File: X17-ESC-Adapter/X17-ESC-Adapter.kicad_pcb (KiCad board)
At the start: 2 copper layers, 9 parts, among them J2 Power In/Out

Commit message: 10/12/24
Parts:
- added J2: Power In/Out, IPS1-105-01-L-D:SAMTEC_IPS1-105-01-L-D, F.Cu at (185.5, 80.0)
- moved ESC3 9.98 mm to (197.0, 87.5), turned to -90 degrees
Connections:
- ESC5 pad 5: ESC2C -> ESC2B
- ESC5 pad 6: ESC2B -> ESC2C
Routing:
- net ESC3C: track 24.3 -> 0.00 mm
- net ESC3B: track 20.4 -> 0.00 mm
- net ESC3A: track 13.5 -> 1.71 mm
- net ESC2C: track 3.77 -> 0.00 mm
- net ESC2B: track 0.00 -> 3.77 mm
- added copper zone on F.Cu, net ESC2A
- added copper zone on F.Cu, net ESC2B
- added copper zone on F.Cu, net ESC2C

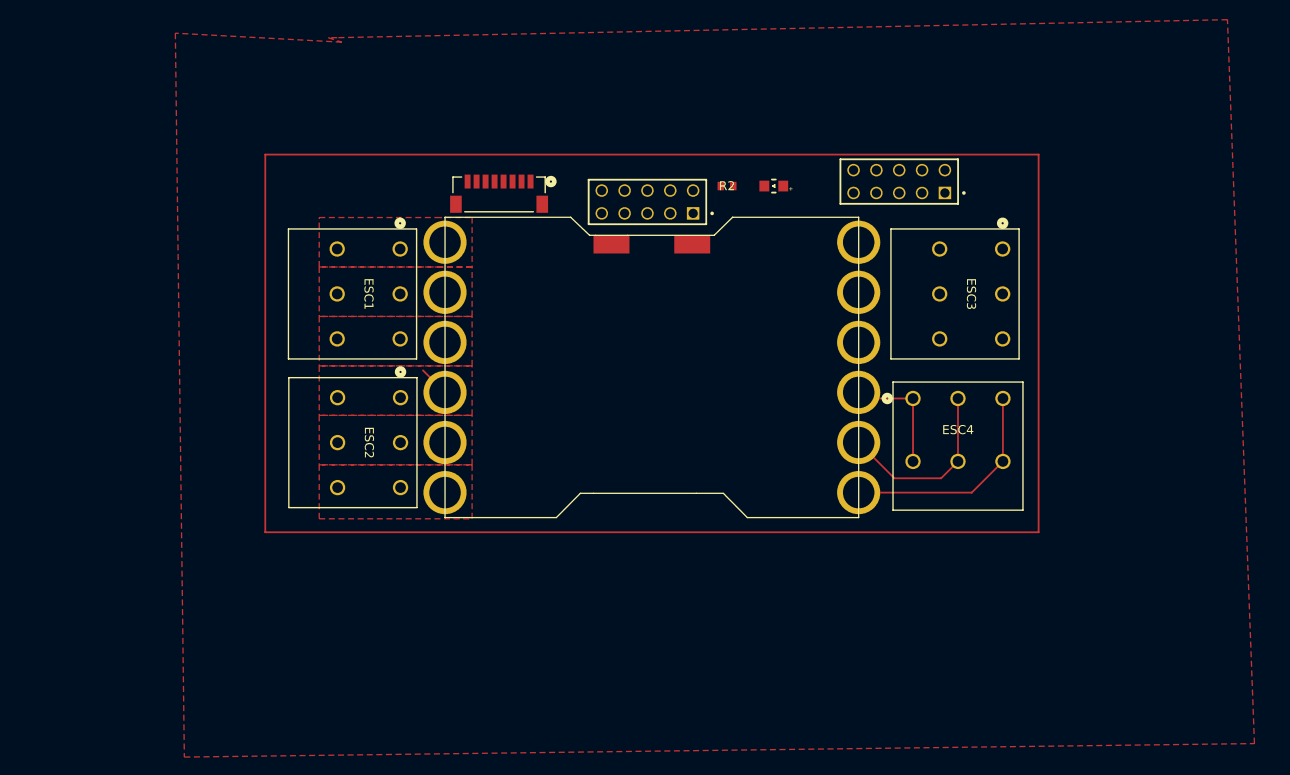
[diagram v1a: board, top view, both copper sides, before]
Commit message: board dimensions
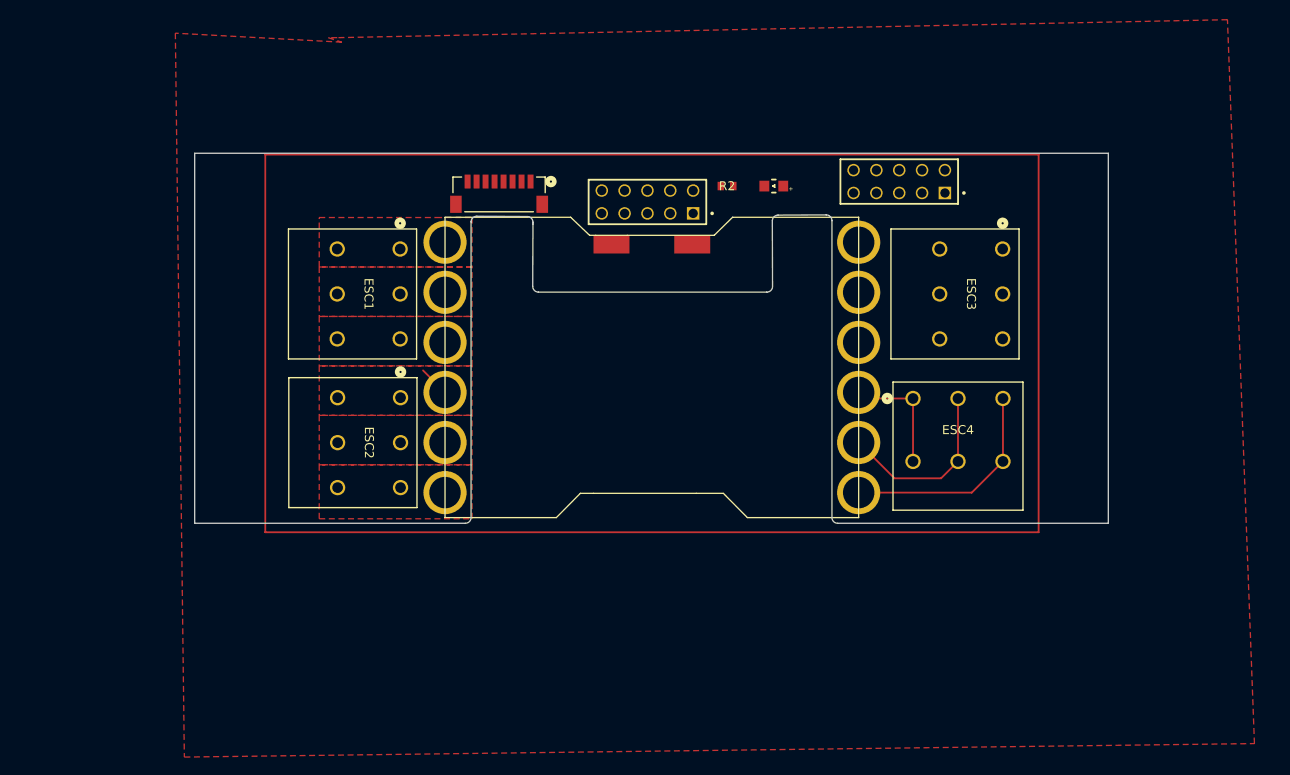
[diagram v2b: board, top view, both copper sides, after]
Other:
- board outline added: 101.6 x 41.1 mm
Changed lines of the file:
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@@
+			)
+		)
+		(property "PARTREV" "R"
+			(at 42.71 -0.225 0)
+			(unlocked yes)
+			(layer "F.Fab")
+			(hide yes)
+			(effects
+				(font
+					(size 1 1)
+					(thickness 0.15)
+				)
+			)
+		)
+		(property "MANUFACTURER" "Samtec"
+			(at 42.71 -0.225 0)
+			(unlocked yes)
+			(layer "F.Fab")
+			(hide yes)
+			(effects
+				(font
+					(size 1 1)
+					(thickness 0.15)
+				)
 			)
 		)
@@
 		(net 9)
 	)
+	(gr_line
+		(start 144.135831 83.888507)
+		(end 138.522431 83.858163)
+		(stroke
+			(width 0.05)
+			(type solid)
+		)
+		(layer "Edge.Cuts")
+	)
+	(gr_line
+		(start 107.15 118)
+		(end 107.15 76.852)
+		(stroke
+			(width 0.05)
+			(type solid)
+		)
+		(layer "Edge.Cuts")
+	)
+	(gr_arc
+		(start 178.651 118)
+		(mid 178.201987 117.814013)
+		(end 178.016 117.365)
+		(stroke
+			(width 0.05)
+			(type solid)
+		)
+		(layer "Edge.Cuts")
+	)
+	(gr_arc
+		(start 145.377459 92.2952)
+		(mid 144.927542 92.108249)
+		(end 144.742465 91.657557)
+		(stroke
+			(width 0.05)
+			(type solid)
+		)
+		(layer "Edge.Cuts")
+	)
+	(gr_line
+		(start 171.410109 91.65806)
+		(end 171.388481 84.369382)
+		(stroke
+			(width 0.05)
+			(type solid)
+		)
+		(layer "Edge.Cuts")
+	)
+	(gr_arc
+		(start 137.883999 84.493154)
+		(mid 138.071145 84.042873)
+		(end 138.522431 83.858163)
+		(stroke
+			(width 0.05)
+			(type solid)
+		)
+		(layer "Edge.Cuts")
+	)
+	(gr_line
+		(start 178.016 84.343285)
+		(end 178.016 117.365)
+		(stroke
+			(width 0.05)
+			(type solid)
+		)
+		(layer "Edge.Cuts")
+	)
+	(gr_line
+		(start 137.249 118)
+		(end 107.15 118)
+		(stroke
+			(width 0.05)
+			(type solid)
+		)
+		(layer "Edge.Cuts")
+	)
+	(gr_line
+		(start 137.884 84.493154)
+		(end 137.884 117.365)
+		(stroke
+			(width 0.05)
+			(type solid)
+		)
+		(layer "Edge.Cuts")
+	)
+	(gr_line
+		(start 178.651 118)
+		(end 208.75 118)
+		(stroke
+			(width 0.05)
+			(type solid)
+		)
+		(layer "Edge.Cuts")
+	)
+	(gr_line
+		(start 144.7674 84.726)
+		(end 144.742465 91.657557)
+		(stroke
+			(width 0.05)
+			(type solid)
+		)
+		(layer "Edge.Cuts")
+	)
+	(gr_line
+		(start 172.020606 83.732532)
+		(end 177.378128 83.708291)
+		(stroke
+			(width 0.05)
+			(type solid)
+		)
+		(layer "Edge.Cuts")
+	)
+	(gr_line
+		(start 144.7674 84.523497)
+		(end 144.7674 84.726)
+		(stroke
+			(width 0.05)
+			(type solid)
+		)
+		(layer "Edge.Cuts")
+	)
+	(gr_line
+		(start 208.75 118)
+		(end 208.75 76.852)
+		(stroke
+			(width 0.05)
+			(type solid)
+		)
+		(layer "Edge.Cuts")
+	)
+	(gr_line
+		(start 145.377459 92.2952)
+		(end 170.775112 92.2952)
+		(stroke
+			(width 0.05)
+			(type solid)
+		)
+		(layer "Edge.Cuts")
+	)
+	(gr_line
+		(start 208.75 76.852)
+		(end 107.15 76.852)
+		(stroke
+			(width 0.05)
+			(type solid)
+		)
+		(layer "Edge.Cuts")
+	)
+	(gr_arc
+		(start 144.135831 83.888507)
+		(mid 144.582654 84.075671)
+		(end 144.767401 84.523498)
+		(stroke
+			(width 0.05)
+			(type solid)
+		)
+		(layer "Edge.Cuts")
+	)
+	(gr_arc
+		(start 177.378128 83.708291)
+		(mid 177.82901 83.893245)
+		(end 178.016 84.343286)
+		(stroke
+			(width 0.05)
+			(type solid)
+		)
+		(layer "Edge.Cuts")
+	)
+	(gr_arc
+		(start 137.884 117.365)
+		(mid 137.698013 117.814013)
+		(end 137.249 118)
+		(stroke
+			(width 0.05)
+			(type solid)
+		)
+		(layer "Edge.Cuts")
+	)
+	(gr_arc
+		(start 171.388481 84.369382)
+		(mid 171.572779 83.92017)
+		(end 172.020606 83.732533)
+		(stroke
+			(width 0.05)
+			(type solid)
+		)
+		(layer "Edge.Cuts")
+	)
+	(gr_arc
+		(start 171.410108 91.658061)
+		(mid 171.224883 92.108459)
+		(end 170.775112 92.2952)
+		(stroke
+			(width 0.05)
+			(type solid)
+		)
+		(layer "Edge.Cuts")
+	)
 	(segment
 		(start 132.54 101)
@@
 		(polygon
 			(pts
-				(xy 121 89.5) (xy 121 95) (xy 138 95) (xy 138 95) (xy 138 89.5) (xy 134.5 89.5)
-			)
-		)
+				(xy 121 89.5) (xy 121 95) (xy 138 95) (xy 138 89.5) (xy 134.5 89.5)
+			)
+		)

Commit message: 10/12/24
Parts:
- removed the J2 at (185.5, 80.0)
- moved ESC4 9.97 mm to (197.0, 104.5), turned to -90 degrees
- moved D1 3.04 mm to (174.6, 81.0), turned to 180 degrees
- moved R2 2.70 mm to (169.0, 81.0)
- moved J2 1.77 mm to (157.5, 80.5)
- moved ESC5 0.50 mm to (135.0, 117.9)
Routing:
- net ESC4C: track 24.5 -> 0.00 mm
- net MTR_1: track 0.00 -> 21.6 mm
- net ESC4B: track 20.5 -> 0.00 mm
- net MTR_2: track 0.00 -> 17.3 mm
- net MTR_3: track 0.00 -> 14.4 mm
- net ESC4A: track 13.3 -> 0.95 mm
- net MTR_4: track 0.00 -> 8.75 mm
- net Net-(D1-Pad2): track 0.00 -> 3.80 mm
- added copper zone on B.Cu, net +12V
- added copper zone on F.Cu, net +12V
- added copper zone on F.Cu, net ESC3A
- added copper zone on F.Cu, net ESC3B
- added copper zone on F.Cu, net ESC3C
- added copper zone on F.Cu, net ESC4A
- added copper zone on F.Cu, net ESC4B
- added copper zone on F.Cu, net ESC4C
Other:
- outline, holes or cut-outs redrawn

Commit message: before design review
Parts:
- added J1: Conn_01x01_Pin, Connector_Wire:SolderWirePad_1x01_SMD_1x2mm, F.Cu at (200.9, 97.8)
- added J1: Conn_01x01_Pin, Connector_Wire:SolderWirePad_1x01_SMD_1x2mm, F.Cu at (201.0, 109.8)
- added J1: Conn_01x01_Pin, Connector_Wire:SolderWirePad_1x01_SMD_1x2mm, F.Cu at (201.0, 114.6)
- added J1: Conn_01x01_Pin, Connector_Wire:SolderWirePad_1x01_SMD_1x2mm, F.Cu at (115.5, 92.5)
- added J1: Conn_01x01_Pin, Connector_Wire:SolderWirePad_1x01_SMD_1x2mm, F.Cu at (115.5, 97.5)
- added J1: Conn_01x01_Pin, Connector_Wire:SolderWirePad_1x01_SMD_1x2mm, F.Cu at (115.5, 114.1)
- added J1: Conn_01x01_Pin, Connector_Wire:SolderWirePad_1x01_SMD_1x2mm, F.Cu at (115.5, 87.1)
- added J1: Conn_01x01_Pin, Connector_Wire:SolderWirePad_1x01_SMD_1x2mm, F.Cu at (200.8, 87.7)
- added J1: Conn_01x01_Pin, Connector_Wire:SolderWirePad_1x01_SMD_1x2mm, F.Cu at (200.9, 104.5)
- added J1: Conn_01x01_Pin, Connector_Wire:SolderWirePad_1x01_SMD_1x2mm, F.Cu at (115.5, 103.5)
- added J1: Conn_01x01_Pin, Connector_Wire:SolderWirePad_1x01_SMD_1x2mm, F.Cu at (200.8, 92.7)
- added J1: Conn_01x01_Pin, Connector_Wire:SolderWirePad_1x01_SMD_1x2mm, F.Cu at (115.5, 108.5)
- J2: value Power In/Out -> Power In (12V)
- moved D1 2.72 mm to (172.3, 79.5), turned to 90 degrees
- moved R2 2.38 mm to (167.6, 79.1), turned to -90 degrees
- moved BM08B-SRSS-TBLFSN1 1.78 mm to (141.0, 79.7), turned to 180 degrees
- moved ESC5 0.82 mm to (134.9, 117.1)
- moved J2 0.47 mm to (158.0, 80.5)
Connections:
- net MTR_1 renamed PWM1
- net MTR_2 renamed PWM2
- net MTR_3 renamed PWM3
- net MTR_4 renamed PWM4
- BM08B-SRSS-TBLFSN1 pad 1: unconnected-(BM08B-SRSS-TBLFSN1-Pad1) -> +5V
- BM08B-SRSS-TBLFSN1 pad 3: unconnected-(BM08B-SRSS-TBLFSN1-Pad3) -> Current ADC
- BM08B-SRSS-TBLFSN1 pad 4: unconnected-(BM08B-SRSS-TBLFSN1-Pad4) -> Telemetry
- J2 pad 05: unconnected-(J2-Pad05) -> +5V
- J2 pad 07: unconnected-(J2-Pad07) -> Current ADC
- J2 pad 09: unconnected-(J2-Pad09) -> Telemetry
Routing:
- net GND: track 0.00 -> 59.9 mm, vias 0 -> 3
- net Current ADC: track 0.00 -> 15.7 mm, vias 0 -> 2
- net +5V: track 0.00 -> 15.0 mm, vias 0 -> 2
- net Telemetry: track 0.00 -> 14.5 mm, vias 0 -> 2
- net PWM1: track 21.6 -> 33.7 mm, vias 0 -> 2
- net PWM4: track 8.75 -> 16.0 mm
- net PWM3: track 14.4 -> 18.2 mm
- net PWM2: track 17.3 -> 20.9 mm
- net Net-(D1-Pad2): track 3.80 -> 5.22 mm
- removed copper zone on B.Cu, net +12V
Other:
- board size 101.6 x 41.1 mm -> 101.6 x 41.2 mm
- board text added: "GND"

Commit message: made some changes
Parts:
- removed the J1 at (200.9, 97.8)
- removed the J1 at (201.0, 109.8)
- removed the J1 at (201.0, 114.6)
- removed the J1 at (115.5, 92.5)
- removed the J1 at (115.5, 97.5)
- removed the J1 at (115.5, 114.1)
- removed the J1 at (115.5, 87.1)
- removed the J1 at (200.8, 87.7)
- removed the J1 at (200.9, 104.5)
- removed the J1 at (115.5, 103.5)
- removed the J1 at (200.8, 92.7)
- removed the J1 at (115.5, 108.5)
- added ?: , , F.Cu at (203.5, 81.0)
- added J1: Pad for ESC, Custom ROV Parts:Pad for ESC Adapter, F.Cu at (112.4, 97.5)
- added J10: Pad for ESC, Custom ROV Parts:Pad for ESC Adapter, F.Cu at (203.4, 92.6)
- added J11: Pad for ESC, Custom ROV Parts:Pad for ESC Adapter, F.Cu at (203.5, 104.6)
- added J12: Pad for ESC, Custom ROV Parts:Pad for ESC Adapter, F.Cu at (203.6, 109.9)
- added J13: Pad for ESC, Custom ROV Parts:Pad for ESC Adapter, F.Cu at (203.5, 114.7)
- added J3: Pad for ESC, Custom ROV Parts:Pad for ESC Adapter, F.Cu at (112.3, 92.3)
- added J4: Pad for ESC, Custom ROV Parts:Pad for ESC Adapter, F.Cu at (112.4, 86.8)
- added J5: Pad for ESC, Custom ROV Parts:Pad for ESC Adapter, F.Cu at (112.4, 113.8)
- added J6: Pad for ESC, Custom ROV Parts:Pad for ESC Adapter, F.Cu at (112.5, 108.9)
- added J7: Pad for ESC, Custom ROV Parts:Pad for ESC Adapter, F.Cu at (112.5, 103.7)
- added J8: Pad for ESC, Custom ROV Parts:Pad for ESC Adapter, F.Cu at (203.4, 87.2)
- added J9: Pad for ESC, Custom ROV Parts:Pad for ESC Adapter, F.Cu at (203.4, 98.0)
- added REF**: 6-32, Custom ROV Parts:6-32, F.Cu at (111.9, 80.7)
- added REF**: 6-32, Custom ROV Parts:6-32, F.Cu at (203.5, 81.0)
- J2: value Power In (12V) -> PWM JST Connector
- moved ESC2 14.3 mm to (119.7, 113.9), turned to 90 degrees
- moved ESC1 13.9 mm to (120.0, 97.2), turned to 90 degrees
- moved ESC3 0.56 mm to (196.4, 87.5)
- moved ESC4 0.54 mm to (196.5, 104.4)
- moved BM08B-SRSS-TBLFSN1 0.20 mm to (140.9, 79.5)
- moved ESC5 0.08 mm to (134.9, 117.0)
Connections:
- ESC1 pad 1: ESC1A -> ESC1C
- ESC1 pad 2: ESC1A -> ESC1C
- ESC1 pad 5: ESC1C -> ESC1A
- ESC1 pad 6: ESC1C -> ESC1A
- ESC2 pad 1: ESC2A -> ESC2C
- ESC2 pad 2: ESC2A -> ESC2C
- ESC2 pad 5: ESC2C -> ESC2A
- ESC2 pad 6: ESC2C -> ESC2A
- J2 pad 04: PWM1 -> PWM4
- J2 pad 05: +5V -> Telemetry
- J2 pad 06: PWM2 -> PWM3
- J2 pad 08: PWM3 -> PWM2
- J2 pad 09: Telemetry -> +5V
- J2 pad 10: PWM4 -> PWM1
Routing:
- net GND: track 59.9 -> 1.19 mm, vias 3 -> 13
- net PWM1: track 33.7 -> 12.3 mm, vias 2 -> 0
- net +12V: track 0.00 -> 10.1 mm
- net PWM4: track 16.0 -> 25.3 mm, vias 0 -> 2
- net +5V: track 15.0 -> 8.01 mm, vias 2 -> 0
- net PWM2: track 20.9 -> 16.9 mm
- net Telemetry: track 14.5 -> 18.3 mm
- net PWM3: track 18.2 -> 20.5 mm
- net ESC2B: track 3.77 -> 1.44 mm
- net Current ADC: track 15.7 -> 13.8 mm, vias 2 -> 0
- added copper zone on B.Cu, net +12V
- added copper zone on B.Cu, net GND
- removed copper zone on F.Cu, net +12V
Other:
- outline, holes or cut-outs redrawn
